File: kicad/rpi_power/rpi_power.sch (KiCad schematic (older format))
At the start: 16 parts, among them J11 RPI_POWER

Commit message: MPD-related improvements
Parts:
- gave numbers to parts that had none: 11
- renumbered C11 to C1, C12 to C2, C13 to C3, D2 to D1, J11 to J1
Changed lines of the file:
@@
 $EndDescr
 $Comp
-L Connector_Generic:Conn_01x04 J11
+L Connector_Generic:Conn_01x04 J1
 U 1 1 5FD578F8
 P 7150 3400
-F 0 "J11" H 7150 3600 50  0000 C CNN
+F 0 "J1" H 7150 3600 50  0000 C CNN
 F 1 "RPI_POWER" V 7250 3350 50  0000 C CNN
 F 2 "Connector_JST:JST_EH_B4B-EH-A_1x04_P2.50mm_Vertical" H 7150 3400 50  0001 C CNN
@@
 Connection ~ 6850 3300
 $Comp
-L power:GNDD #PWR06
+L power:GNDD #PWR07
 U 1 1 5FD57DA6
 P 6850 3650
-F 0 "#PWR06" H 6850 3400 50  0001 C CNN
+F 0 "#PWR07" H 6850 3400 50  0001 C CNN
 F 1 "GNDD" H 6854 3495 50  0000 C CNN
 F 2 "" H 6850 3650 50  0001 C CNN
@@
 Connection ~ 6850 3600
 $Comp
-L Device:CP_Small C12
+L Device:CP_Small C2
 U 1 1 5FD57DCE
 P 6050 2650
-F 0 "C12" H 6138 2696 50  0000 L CNN
+F 0 "C2" H 6138 2696 50  0000 L CNN
 F 1 "470.0" H 6138 2605 50  0000 L CNN
 F 2 "Capacitor_THT:CP_Radial_D10.0mm_P5.00mm" H 6050 2650 50  0001 C CNN
@@
 	6050 3000 6450 3000
 $Comp
-L Device:C_Small C13
+L Device:C_Small C3
 U 1 1 5FD57DE0
 P 6450 2650
-F 0 "C13" H 6542 2696 50  0000 L CNN
+F 0 "C3" H 6542 2696 50  0000 L CNN
 F 1 "0.1" H 6542 2605 50  0000 L CNN
 F 2 "Capacitor_THT:C_Rect_L7.0mm_W3.5mm_P5.00mm" H 6450 2650 50  0001 C CNN
@@
 	5150 3100 5150 3000
 $Comp
-L power:GNDD #PWR04
+L power:GNDD #PWR05
 U 1 1 5FD57E09
 P 5750 3100
-F 0 "#PWR04" H 5750 2850 50  0001 C CNN
+F 0 "#PWR05" H 5750 2850 50  0001 C CNN
 F 1 "GNDD" H 5754 2945 50  0000 C CNN
 F 2 "" H 5750 3100 50  0001 C CNN
@@
 Connection ~ 4100 2300
 $Comp
-L Transistor_FET:IRLML5203 Q?
+L Transistor_FET:IRLML5203 Q2
 U 1 1 603CB87C
 P 4550 2400
-F 0 "Q?" V 4892 2400 50  0000 C CNN
+F 0 "Q2" V 4892 2400 50  0000 C CNN
 F 1 "IRLML5203" V 4801 2400 50  0000 C CNN
 F 2 "Package_TO_SOT_SMD:SOT-23" H 4750 2325 50  0001 L CIN
@@
 $EndComp
 $Comp
-L Device:R R?
+L Device:R R2
 U 1 1 60410A16
 P 4100 2500
-F 0 "R?" H 4000 2450 50  0000 C CNN
+F 0 "R2" H 4000 2450 50  0000 C CNN
 F 1 "100k" H 3950 2550 50  0000 C CNN
 F 2 "Resistor_SMD:R_1206_3216Metric_Pad1.30x1.75mm_HandSolder" V 4030 2500 50  0001 C CNN
@@
 $EndComp
 $Comp
-L Device:R R?
+L Device:R R3
 U 1 1 60411DEB
 P 4550 2800
-F 0 "R?" H 4450 2750 50  0000 C CNN
+F 0 "R3" H 4450 2750 50  0000 C CNN
 F 1 "100k" H 4400 2850 50  0000 C CNN
 F 2 "Resistor_SMD:R_1206_3216Metric_Pad1.30x1.75mm_HandSolder" V 4480 2800 50  0001 C CNN
@@
 	4100 2650 4100 3400
 $Comp
-L Transistor_FET:IRLML0030 Q?
+L Transistor_FET:IRLML0030 Q1
 U 1 1 60482082
 P 4450 3800
-F 0 "Q?" H 4654 3846 50  0000 L CNN
+F 0 "Q1" H 4654 3846 50  0000 L CNN
 F 1 "IRLML6244" H 4654 3755 50  0000 L CNN
 F 2 "Package_TO_SOT_SMD:SOT-23" H 4650 3725 50  0001 L CIN
@@
 	4550 4200 4550 4000
 $Comp
-L Device:R R?
+L Device:R R1
 U 1 1 604F5B01
 P 4050 4000
-F 0 "R?" H 3950 3950 50  0000 C CNN
+F 0 "R1" H 3950 3950 50  0000 C CNN
 F 1 "100k" H 3900 4050 50  0000 C CNN
 F 2 "Resistor_SMD:R_1206_3216Metric_Pad1.30x1.75mm_HandSolder" V 3980 4000 50  0001 C CNN
@@
 	4050 3800 3750 3800
 $Comp
-L power:GNDD #PWR?
+L power:GNDD #PWR02
 U 1 1 604D697C
 P 4550 4200
-F 0 "#PWR?" H 4550 3950 50  0001 C CNN
+F 0 "#PWR02" H 4550 3950 50  0001 C CNN
 F 1 "GNDD" H 4554 4045 50  0000 C CNN
 F 2 "" H 4550 4200 50  0001 C CNN
@@
 $EndComp
 $Comp
-L power:GNDD #PWR?
+L power:GNDD #PWR01
 U 1 1 605068A4
 P 4050 4200
-F 0 "#PWR?" H 4050 3950 50  0001 C CNN
+F 0 "#PWR01" H 4050 3950 50  0001 C CNN
 F 1 "GNDD" H 4054 4045 50  0000 C CNN
 F 2 "" H 4050 4200 50  0001 C CNN
@@
 	2900 2300 2950 2300
 $Comp
-L Device:CP_Small C11
+L Device:CP_Small C1
 U 1 1 5FD57DBF
 P 3650 2750
-F 0 "C11" H 3738 2796 50  0000 L CNN
+F 0 "C1" H 3738 2796 50  0000 L CNN
 F 1 "1000.0" H 3738 2705 50  0000 L CNN
 F 2 "Capacitor_THT:CP_Radial_D10.0mm_P5.00mm_P7.50mm" H 3650 2750 50  0001 C CNN
@@
 	4050 3800 4250 3800
 $Comp
-L Transistor_FET:IRLML0030 Q?
+L Transistor_FET:IRLML0030 Q3
 U 1 1 605FA4E1
 P 5350 3700
-F 0 "Q?" H 5555 3746 50  0000 L CNN
+F 0 "Q3" H 5555 3746 50  0000 L CNN
 F 1 "IRLML6244" H 5555 3655 50  0000 L CNN
 F 2 "Package_TO_SOT_SMD:SOT-23" H 5550 3625 50  0001 L CIN
@@
 $EndComp
 $Comp
-L power:GNDD #PWR?
+L power:GNDD #PWR04
 U 1 1 6060E085
 P 5250 4200
-F 0 "#PWR?" H 5250 3950 50  0001 C CNN
+F 0 "#PWR04" H 5250 3950 50  0001 C CNN
 F 1 "GNDD" H 5254 4045 50  0000 C CNN
 F 2 "" H 5250 4200 50  0001 C CNN
@@
 	5250 3400 5250 3500
 $Comp
-L Transistor_FET:IRLML0030 Q?
+L Transistor_FET:IRLML0030 Q4
 U 1 1 6062F31C
 P 6000 3950
-F 0 "Q?" H 6205 3996 50  0000 L CNN
+F 0 "Q4" H 6205 3996 50  0000 L CNN
 F 1 "IRLML6244" H 6205 3905 50  0000 L CNN
 F 2 "Package_TO_SOT_SMD:SOT-23" H 6200 3875 50  0001 L CIN
@@
 	5900 3700 5900 3750
 $Comp
-L power:GNDD #PWR?
+L power:GNDD #PWR06
 U 1 1 606442E7
 P 5900 4200
-F 0 "#PWR?" H 5900 3950 50  0001 C CNN
+F 0 "#PWR06" H 5900 3950 50  0001 C CNN
 F 1 "GNDD" H 5904 4045 50  0000 C CNN
 F 2 "" H 5900 4200 50  0001 C CNN
@@
 	6200 3950 6350 3950
 $Comp
-L Device:R R?
+L Device:R R4
 U 1 1 60676FD1
 P 5900 3500
-F 0 "R?" H 5800 3450 50  0000 C CNN
+F 0 "R4" H 5800 3450 50  0000 C CNN
 F 1 "100k" H 5750 3550 50  0000 C CNN
 F 2 "Resistor_SMD:R_1206_3216Metric_Pad1.30x1.75mm_HandSolder" V 5830 3500 50  0001 C CNN
@@
 	5900 3350 5900 3300
 $Comp
-L Diode_Bridge:GBU8K D2
+L Diode_Bridge:GBU8K D1
 U 1 1 5FD57DB5
 P 3250 2300
-F 0 "D2" H 3400 2550 50  0000 L CNN
+F 0 "D1" H 3400 2550 50  0000 L CNN
 F 1 "GBU8K" H 3400 2450 50  0000 L CNN
 F 2 "Diode_THT:Diode_Bridge_Vishay_GBU" H 3400 2425 50  0001 L CNN
@@
 	6850 2300 6850 3300
 $Comp
-L Device:R R?
+L Device:R R5
 U 1 1 608EA7AA
 P 6350 3500
-F 0 "R?" H 6250 3450 50  0000 C CNN
+F 0 "R5" H 6250 3450 50  0000 C CNN
 F 1 "100k" H 6200 3550 50  0000 C CNN
 F 2 "Resistor_SMD:R_1206_3216Metric_Pad1.30x1.75mm_HandSolder" V 6280 3500 50  0001 C CNN
@@
 	3650 3000 5150 3000
 $Comp
-L Connector_Generic:Conn_01x02 J?
+L Connector_Generic:Conn_01x02 J2
 U 1 1 603E8660
 P 7150 3950
-F 0 "J?" H 7100 4050 50  0000 L CNN
+F 0 "J2" H 7100 4050 50  0000 L CNN
 F 1 "RPI_OFF" V 7250 3750 50  0000 L CNN
 F 2 "" H 7150 3950 50  0001 C CNN
@@
 Connection ~ 6350 3950
 $Comp
-L power:GNDD #PWR?
+L power:GNDD #PWR08
 U 1 1 603EB0D7
 P 6850 4200
-F 0 "#PWR?" H 6850 3950 50  0001 C CNN
+F 0 "#PWR08" H 6850 3950 50  0001 C CNN
 F 1 "GNDD" H 6854 4045 50  0000 C CNN
 F 2 "" H 6850 4200 50  0001 C CNN
@@
 	6350 3650 6350 3950
 $Comp
-L ampcontrol-f103:XL4015_module U?
+L ampcontrol-f103:XL4015_module U1
 U 1 1 603BCAE3
 P 5450 2550
-F 0 "U?" H 5450 3065 50  0000 C CNN
+F 0 "U1" H 5450 3065 50  0000 C CNN
 F 1 "XL4015_module" H 5450 2974 50  0000 C CNN
 F 2 "" H 5750 2950 50  0001 C CNN

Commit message: Fix rpi-power schematics
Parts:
- R5: value 100k -> 10k
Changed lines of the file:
@@
 P 4100 2500
 F 0 "R2" H 4000 2450 50  0000 C CNN
-F 1 "100k" H 3950 2550 50  0000 C CNN
+F 1 "100k" H 3850 2550 50  0000 L CNN
 F 2 "Resistor_SMD:R_1206_3216Metric_Pad1.30x1.75mm_HandSolder" V 4030 2500 50  0001 C CNN
 F 3 "~" H 4100 2500 50  0001 C CNN
@@
 P 4550 2800
 F 0 "R3" H 4450 2750 50  0000 C CNN
-F 1 "100k" H 4400 2850 50  0000 C CNN
+F 1 "100k" H 4300 2850 50  0000 L CNN
 F 2 "Resistor_SMD:R_1206_3216Metric_Pad1.30x1.75mm_HandSolder" V 4480 2800 50  0001 C CNN
 F 3 "~" H 4550 2800 50  0001 C CNN
@@
 P 5900 3500
 F 0 "R4" H 5800 3450 50  0000 C CNN
-F 1 "100k" H 5750 3550 50  0000 C CNN
+F 1 "100k" H 5650 3550 50  0000 L CNN
 F 2 "Resistor_SMD:R_1206_3216Metric_Pad1.30x1.75mm_HandSolder" V 5830 3500 50  0001 C CNN
 F 3 "~" H 5900 3500 50  0001 C CNN
@@
 P 6350 3500
 F 0 "R5" H 6250 3450 50  0000 C CNN
-F 1 "100k" H 6200 3550 50  0000 C CNN
+F 1 "10k" H 6150 3550 50  0000 L CNN
 F 2 "Resistor_SMD:R_1206_3216Metric_Pad1.30x1.75mm_HandSolder" V 6280 3500 50  0001 C CNN
 F 3 "~" H 6350 3500 50  0001 C CNN

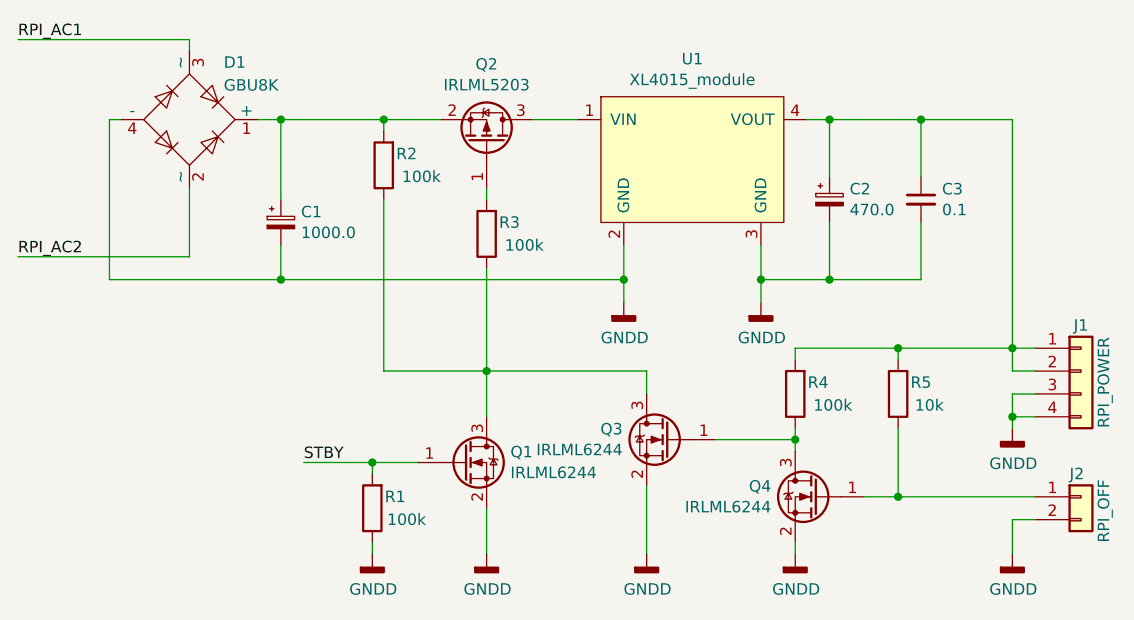
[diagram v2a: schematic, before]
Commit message: Modify rpi_power schematic
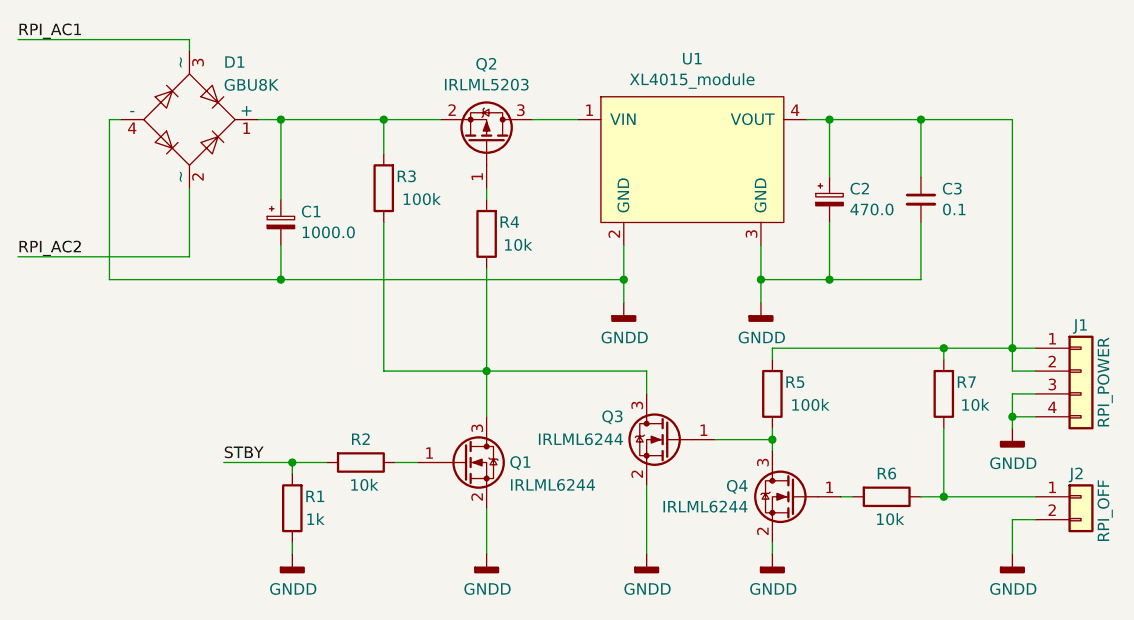
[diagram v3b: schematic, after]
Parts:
- added R2, R6: 10k, Resistor_SMD:R_1206_3216Metric_Pad1.30x1.75mm_HandSolder, symbol Device:R
- R1: value 100k -> 1k
- R4: renamed from R3; value 100k -> 10k
- renumbered R2 to R3, R4 to R5, R5 to R7
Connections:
- net STBY: now also R2.2; no longer Q1.1 (G)
- net at J2.1 (Pin_1), R7.1: now also R6.1; no longer Q4.1 (G)
- new net: Q4.1 (G), R6.2
- new net: Q1.1 (G), R2.1
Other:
- moved on the sheet: Q4, R1, R3, R5, R7
